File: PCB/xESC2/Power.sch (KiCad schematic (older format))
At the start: 0 parts

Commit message: power schematic wip
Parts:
- added C10, C8, C9: 470nF/16V, Capacitor_SMD:C_0603_1608Metric, symbol Device:C
- added C11: 22nF/100V, Capacitor_SMD:C_0603_1608Metric, symbol Device:C
- added C12, C13, C14: 100nF/100V, Capacitor_SMD:C_0805_2012Metric, symbol Device:C
- added C4, C5: 2.2uF/50V, Capacitor_SMD:C_0805_2012Metric, symbol Device:C
- added C6, C7: 100nF/50V, Capacitor_SMD:C_0603_1608Metric, symbol Device:C
- added R13, R14, R15: DNP, Resistor_SMD:R_0603_1608Metric, symbol Device:R
- added U1: TMC6200-TA, footprints:TMC6200-TA, symbol 2021-11-28_18-58-59:TMC6200-TA
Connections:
- new net: C11.1, U1.30 (CPO)
- new net: C11.2, U1.32 (CPI)
- new net: C12.1, U1.34 (VCP)
- new net: C5.2, U1.6 (12VOUT)
- new net 5VOUT: C4.2, R15.1, U1.7 (5VOUT)
- new net CU: C8.2, U1.1 (CU)
- new net CURU_5V: U1.9 (CURU)
- new net CURV_5V: U1.10 (CURV)
- new net CURW_5V: U1.11 (CURW)
- new net CV: C9.2, U1.44 (CV)
- new net CW: C10.2, U1.36 (CW)
- new net DRV_ENABLE: U1.27 (DRV_EN)
- new net DRV_U: C8.1, U1.47 (U)
- new net DRV_V: C9.1, U1.42 (V)
- new net DRV_W: C10.1, U1.38 (W)
- new net FAULT: U1.26 (FAULT)
- new net GND: C13.2, C14.2, C4.1, C5.1, C6.2, C7.2, R14.2, U1.24 (CLK), U1.8 (GNDA), U1.EPAD
- new net HSU: U1.48 (HSU)
- new net HSV: U1.43 (HSV)
- new net HSW: U1.37 (HSW)
- new net LSU: U1.5 (LSU)
- new net LSV: U1.4 (LSV)
- new net LSW: U1.3 (LSW)
- new net MISO: U1.16 (SDO_SINGLE)
- new net MOSI: U1.15 (SDI_AMPLX10)
- new net NCS: U1.13 (CSN_IDRV0)
- new net SCK: U1.14 (SCK_IDRV1)
- new net SENSE_U: U1.46 (USENSE)
- new net SENSE_V: U1.41 (VSENSE)
- new net SENSE_W: U1.39 (WSENSE)
- new net UH: U1.17 (UH)
- new net UL: U1.18 (UL)
- new net VCCIO: C7.1, R13.1, U1.19 (VCC_IO), U1.25 (SPE)
- new net VH: U1.20 (VH)
- new net VL: U1.21 (VL)
- new net VM: C12.2, C13.1, C14.1, U1.29 (VSA), U1.33 (VS)
- new net VOFS: C6.1, R13.2, R14.1, R15.2, U1.12 (VOFS/TEST)
- new net WH: U1.22 (WH)
- new net WL: U1.23 (WL)

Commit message: wip
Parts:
- added C15, C16, C17: 1uF/50V, Capacitor_SMD:C_0805_2012Metric, symbol Device:C
- added C18: 100uF/16V, Capacitor_SMD:CP_Elec_6.3x7.7, symbol Device:CP
- added C19, C20: 10uF/25V, Capacitor_SMD:C_1206_3216Metric, symbol Device:C
- added C21: 47uF/100V, Capacitor_THT:CP_Radial_D8.0mm_P3.50mm, symbol Device:CP
- added C22, C23: 220uF/63V, Capacitor_THT:CP_Radial_D10.0mm_P5.00mm_P7.50mm, symbol Device:CP
- added D1: SS36, Diode_SMD:D_SMA, symbol Device:D_Schottky
- added D2: LED, LED_SMD:LED_0603_1608Metric, symbol Device:LED
- added L1: 47uH/3A, Inductor_SMD:L_Wuerth_HCI-1040, symbol Device:L
- added R16: 150R, Resistor_SMD:R_0603_1608Metric, symbol Device:R
- added TP4, TP5, TP6, TP7: TestPoint, TestPoint:TestPoint_Pad_4.0x4.0mm, symbol Connector:TestPoint
- added U2: XL2001, Package_SO:SOP-8_3.9x4.9mm_P1.27mm, symbol xESC2:XL2001
- added U3: AMS1117-3.3, Package_TO_SOT_SMD:SOT-223-3_TabPin2, symbol Regulator_Linear:AMS1117-3.3
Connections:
- net FAULT: now also R16.1
- net GND: now also C16.2, C17.2, C18.2, C19.2, C20.2, C21.2, C22.2, C23.2, D1.2 (A), D2.1 (K), TP6.1, TP7.1, U2.7 (GND), U2.8 (GND), U3.1 (GND)
- net VM: now also C15.2, C16.1, C21.1, C22.1, C23.1, TP4.1, TP5.1, U2.4 (VIN)
- new net: C15.1, U2.3 (VC)
- new net: D1.1 (K), L1.1, U2.5 (SW), U2.6 (SW)
- new net: D2.2 (A), R16.2
- new net 3V3_OUT: C20.1, U3.2 (VO)
- new net 5V_OUT: C17.1, C18.1, C19.1, L1.2, U2.1 (FB), U3.3 (VI)
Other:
- note added: "5V DC/DC Regulator"
- note added: "Optional 3.3V LDO"
- moved on the sheet: C10, C11, C12, C13, C14, C4, C5, C6, C7, C8, C9, R13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

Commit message: wip power xESC2
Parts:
- removed C15, C16, C17: 1uF/50V, Capacitor_SMD:C_0805_2012Metric, symbol Device:C
- removed C18: 100uF/16V, Capacitor_SMD:CP_Elec_6.3x7.7, symbol Device:CP
- removed C19, C20: 10uF/25V, Capacitor_SMD:C_1206_3216Metric, symbol Device:C
- removed C21: 47uF/100V, Capacitor_THT:CP_Radial_D8.0mm_P3.50mm, symbol Device:CP
- removed D1: SS36, Diode_SMD:D_SMA, symbol Device:D_Schottky
- removed L1: 47uH/3A, Inductor_SMD:L_Wuerth_HCI-1040, symbol Device:L
- removed U2: XL2001, Package_SO:SOP-8_3.9x4.9mm_P1.27mm, symbol xESC2:XL2001
- removed U3: AMS1117-3.3, Package_TO_SOT_SMD:SOT-223-3_TabPin2, symbol Regulator_Linear:AMS1117-3.3
- TP4, TP5, TP6, TP7: footprint TestPoint:TestPoint_Pad_4.0x4.0mm -> xESC2:SolderPadHighCurrent
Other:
- note removed: "5V DC/DC Regulator"
- note removed: "Optional 3.3V LDO"

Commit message: wip logic
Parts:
- added C44: 100nF/50V, Capacitor_SMD:C_0603_1608Metric, symbol Device:C
- added R29, R31: 10k, Resistor_SMD:R_0603_1608Metric, symbol Device:R
- added R30: 10k NTC, Resistor_SMD:R_0603_1608Metric, symbol Device:R
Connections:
- net DRV_ENABLE: now also R29.1
- net GND: now also C44.2, R29.2, R31.2
- net VCCIO: now also R30.1
- net DRV_U renamed PHASE_U
- net DRV_V renamed PHASE_V
- net DRV_W renamed PHASE_W
- new net TEMP: C44.1, R30.2, R31.1
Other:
- moved on the sheet: C13
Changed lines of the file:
@@
 	5800 1050 6150 1050
 Wire Wire Line
-	6150 1050 6150 3700
+	6150 1050 6150 3950
 $Comp
 L power:GND #PWR0107
@@
 	6600 2650 5800 2650
 Wire Wire Line
-	6750 2700 7050 2700
+	6750 2700 7300 2700
 Connection ~ 6750 2700
 $Comp
@@
 	7450 2700 9300 2700
 Wire Wire Line
-	7450 3100 7450 3700
-Wire Wire Line
-	7450 3700 7050 3700
-Connection ~ 6150 3700
-Wire Wire Line
-	6150 3700 6150 4100
+	7450 3100 7450 3950
+Wire Wire Line
+	7450 3950 7300 3950
+Connection ~ 6150 3950
+Wire Wire Line
+	6150 3950 6150 4100
 $Comp
 L Device:C C6
@@
 L Device:C C13
 U 1 1 61AC2597
-P 7050 3300
-F 0 "C13" H 7165 3346 50  0000 L CNN
-F 1 "100nF/100V" H 7165 3255 50  0000 L CNN
-F 2 "Capacitor_SMD:C_0805_2012Metric" H 7088 3150 50  0001 C CNN
-F 3 "~" H 7050 3300 50  0001 C CNN
-	1    7050 3300
-	1    0    0    -1
-$EndComp
-Wire Wire Line
-	5800 3050 7050 3050
-Wire Wire Line
-	7050 3050 7050 3150
-Wire Wire Line
-	7050 3450 7050 3700
-Connection ~ 7050 3700
-Wire Wire Line
-	7050 3700 6150 3700
-Wire Wire Line
-	7050 3050 7050 2700
-Connection ~ 7050 3050
-Connection ~ 7050 2700
-Wire Wire Line
-	7050 2700 7450 2700
-Text HLabel 6300 3250 2    50   Input ~ 0
+P 7300 3300
+F 0 "C13" H 7415 3346 50  0000 L CNN
+F 1 "100nF/100V" H 7415 3255 50  0000 L CNN
+F 2 "Capacitor_SMD:C_0805_2012Metric" H 7338 3150 50  0001 C CNN
+F 3 "~" H 7300 3300 50  0001 C CNN
+	1    7300 3300
+	1    0    0    -1
+$EndComp
+Wire Wire Line
+	5800 3050 7300 3050
+Wire Wire Line
+	7300 3050 7300 3150
+Wire Wire Line
+	7300 3450 7300 3950
+Connection ~ 7300 3950
+Wire Wire Line
+	7300 3950 6600 3950
+Wire Wire Line
+	7300 3050 7300 2700
+Connection ~ 7300 3050
+Connection ~ 7300 2700
+Wire Wire Line
+	7300 2700 7450 2700
+Text HLabel 6650 3250 2    50   Input ~ 0
 DRV_ENABLE
 Wire Wire Line
-	6300 3250 5800 3250
-Wire Wire Line
-	5800 3450 6300 3450
+	6650 3250 6600 3250
+Wire Wire Line
+	5800 3450 6050 3450
 Wire Wire Line
 	3400 2250 1000 2250
@@
 Text Label 2350 2850 0    50   ~ 0
 VCCIO
-Text Label 6300 3450 2    50   ~ 0
+Text Label 6050 3450 2    50   ~ 0
 VCCIO
 Text Label 7950 4950 2    50   ~ 0
@@
 Text Label 950  4750 3    50   ~ 0
 VM
+Text HLabel 9050 2200 0    50   Output ~ 0
+PHASE_U
+Text HLabel 9050 3450 0    50   Output ~ 0
+PHASE_V
+Text HLabel 9050 4700 0    50   Output ~ 0
+PHASE_W
+Connection ~ 6600 3250
+Wire Wire Line
+	6600 3250 5800 3250
+$Comp
+L Device:R R29
+U 1 1 61BF62F2
+P 6600 3700
+F 0 "R29" H 6670 3746 50  0000 L CNN
+F 1 "10k" H 6670 3655 50  0000 L CNN
+F 2 "Resistor_SMD:R_0603_1608Metric" V 6530 3700 50  0001 C CNN
+F 3 "~" H 6600 3700 50  0001 C CNN
+	1    6600 3700
+	1    0    0    -1
+$EndComp
+Wire Wire Line
+	6600 3250 6600 3550
+Wire Wire Line
+	6600 3850 6600 3950
+Connection ~ 6600 3950
+Wire Wire Line
+	6600 3950 6150 3950
+$Comp
+L Device:R R30
+U 1 1 61C1EF32
+P 6300 5300
+F 0 "R30" H 6370 5346 50  0000 L CNN
+F 1 "10k NTC" H 6370 5255 50  0000 L CNN
+F 2 "Resistor_SMD:R_0603_1608Metric" V 6230 5300 50  0001 C CNN
+F 3 "~" H 6300 5300 50  0001 C CNN
+	1    6300 5300
+	1    0    0    -1
+$EndComp
+$Comp
+L Device:R R31
+U 1 1 61C1EF38
+P 6300 5850
+F 0 "R31" H 6370 5896 50  0000 L CNN
+F 1 "10k" H 6370 5805 50  0000 L CNN
+F 2 "Resistor_SMD:R_0603_1608Metric" V 6230 5850 50  0001 C CNN
+F 3 "~" H 6300 5850 50  0001 C CNN
+	1    6300 5850
+	1    0    0    -1
+$EndComp
+Wire Wire Line
+	6300 5700 6300 5550
+Connection ~ 6300 5550
+Wire Wire Line
+	6300 5550 6300 5450
+Wire Wire Line
+	6300 5150 6300 4950
+Wire Wire Line
+	6300 5550 6650 5550
+Text Label 6300 4950 2    50   ~ 0
+VCCIO
+$Comp
+L power:GND #PWR0133
+U 1 1 61C25A4C
+P 6300 6200
+F 0 "#PWR0133" H 6300 5950 50  0001 C CNN
+F 1 "GND" H 6305 6027 50  0000 C CNN
+F 2 "" H 6300 6200 50  0001 C CNN
+F 3 "" H 6300 6200 50  0001 C CNN
+	1    6300 6200
+	1    0    0    -1
+$EndComp
+Wire Wire Line
+	6300 6000 6300 6150
+Text HLabel 6650 5550 2    50   Output ~ 0
+TEMP
+$Comp
+L Device:C C44
+U 1 1 61C2CC0D
+P 5650 5850
+F 0 "C44" H 5765 5896 50  0000 L CNN
+F 1 "100nF/50V" H 5765 5805 50  0000 L CNN
+F 2 "Capacitor_SMD:C_0603_1608Metric" H 5688 5700 50  0001 C CNN
+F 3 "~" H 5650 5850 50  0001 C CNN
+	1    5650 5850
+	1    0    0    -1
+$EndComp
+Wire Wire Line
+	6300 5550 5650 5550
+Wire Wire Line
+	5650 5550 5650 5700
+Wire Wire Line
+	5650 6000 5650 6150
+Wire Wire Line
+	5650 6150 6300 6150
+Connection ~ 6300 6150
+Wire Wire Line
+	6300 6150 6300 6200
 $EndSCHEMATC

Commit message: wip V2.0
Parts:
- removed C44: 100nF/50V, Capacitor_SMD:C_0603_1608Metric, symbol Device:C
- removed R30: 10k NTC, Resistor_SMD:R_0603_1608Metric, symbol Device:R
- removed R31: 10k, Resistor_SMD:R_0603_1608Metric, symbol Device:R
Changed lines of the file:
@@
 encoding utf-8
 Sheet 2 7
-Title ""
-Date ""
-Rev ""
-Comp ""
-Comment1 ""
-Comment2 ""
+Title "xESC BLDC Controller"
+Date "2021-12-01"
+Rev "2.0"
+Comp "Clemens Elflein"
+Comment1 "Creative Commons Attribution-NonCommercial-ShareAlike 4.0 International License."
+Comment2 "Licensed under "
 Comment3 ""
 Comment4 ""
@@
 Wire Wire Line
 	6600 3950 6150 3950
-$Comp
-L Device:R R30
-U 1 1 61C1EF32
-P 6300 5300
-F 0 "R30" H 6370 5346 50  0000 L CNN
-F 1 "10k NTC" H 6370 5255 50  0000 L CNN
-F 2 "Resistor_SMD:R_0603_1608Metric" V 6230 5300 50  0001 C CNN
-F 3 "~" H 6300 5300 50  0001 C CNN
-	1    6300 5300
-	1    0    0    -1
-$EndComp
-$Comp
-L Device:R R31
-U 1 1 61C1EF38
-P 6300 5850
-F 0 "R31" H 6370 5896 50  0000 L CNN
-F 1 "10k" H 6370 5805 50  0000 L CNN
-F 2 "Resistor_SMD:R_0603_1608Metric" V 6230 5850 50  0001 C CNN
-F 3 "~" H 6300 5850 50  0001 C CNN
-	1    6300 5850
-	1    0    0    -1
-$EndComp
-Wire Wire Line
-	6300 5700 6300 5550
-Connection ~ 6300 5550
-Wire Wire Line
-	6300 5550 6300 5450
-Wire Wire Line
-	6300 5150 6300 4950
-Wire Wire Line
-	6300 5550 6650 5550
-Text Label 6300 4950 2    50   ~ 0
-VCCIO
-$Comp
-L power:GND #PWR0133
-U 1 1 61C25A4C
-P 6300 6200
-F 0 "#PWR0133" H 6300 5950 50  0001 C CNN
-F 1 "GND" H 6305 6027 50  0000 C CNN
-F 2 "" H 6300 6200 50  0001 C CNN
-F 3 "" H 6300 6200 50  0001 C CNN
-	1    6300 6200
-	1    0    0    -1
-$EndComp
-Wire Wire Line
-	6300 6000 6300 6150
-Text HLabel 6650 5550 2    50   Output ~ 0
-TEMP
-$Comp
-L Device:C C44
-U 1 1 61C2CC0D
-P 5650 5850
-F 0 "C44" H 5765 5896 50  0000 L CNN
-F 1 "100nF/50V" H 5765 5805 50  0000 L CNN
-F 2 "Capacitor_SMD:C_0603_1608Metric" H 5688 5700 50  0001 C CNN
-F 3 "~" H 5650 5850 50  0001 C CNN
-	1    5650 5850
-	1    0    0    -1
-$EndComp
-Wire Wire Line
-	6300 5550 5650 5550
-Wire Wire Line
-	5650 5550 5650 5700
-Wire Wire Line
-	5650 6000 5650 6150
-Wire Wire Line
-	5650 6150 6300 6150
-Connection ~ 6300 6150
-Wire Wire Line
-	6300 6150 6300 6200
 $EndSCHEMATC

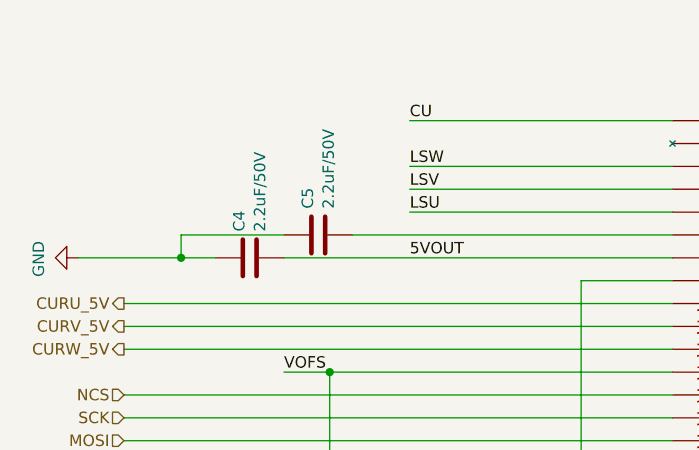
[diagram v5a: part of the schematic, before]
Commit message: changed some values, added BOM
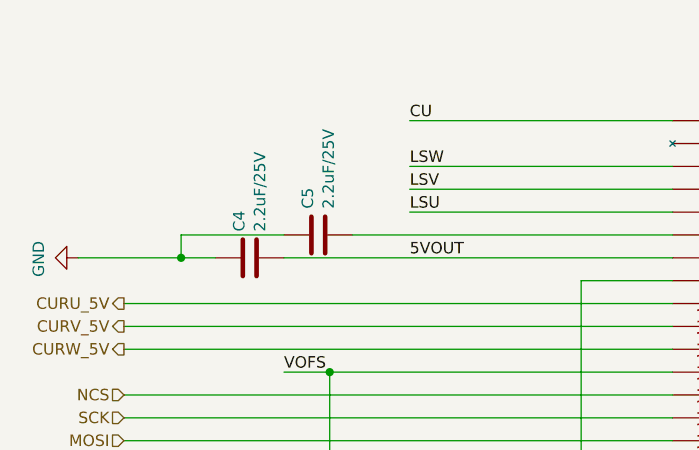
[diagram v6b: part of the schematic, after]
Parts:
- C4, C5: value 2.2uF/50V -> 2.2uF/25V
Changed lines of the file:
@@
 P 1550 1650
 F 0 "C4" H 1665 1696 50  0000 L CNN
-F 1 "2.2uF/50V" H 1665 1605 50  0000 L CNN
+F 1 "2.2uF/25V" H 1665 1605 50  0000 L CNN
 F 2 "Capacitor_SMD:C_0805_2012Metric" H 1588 1500 50  0001 C CNN
 F 3 "~" H 1550 1650 50  0001 C CNN
@@
 P 1850 1550
 F 0 "C5" H 1965 1596 50  0000 L CNN
-F 1 "2.2uF/50V" H 1965 1505 50  0000 L CNN
+F 1 "2.2uF/25V" H 1965 1505 50  0000 L CNN
 F 2 "Capacitor_SMD:C_0805_2012Metric" H 1888 1400 50  0001 C CNN
 F 3 "~" H 1850 1550 50  0001 C CNN
